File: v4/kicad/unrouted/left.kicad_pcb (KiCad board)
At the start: 2 copper layers, 160 x 118.6 mm, 68 parts

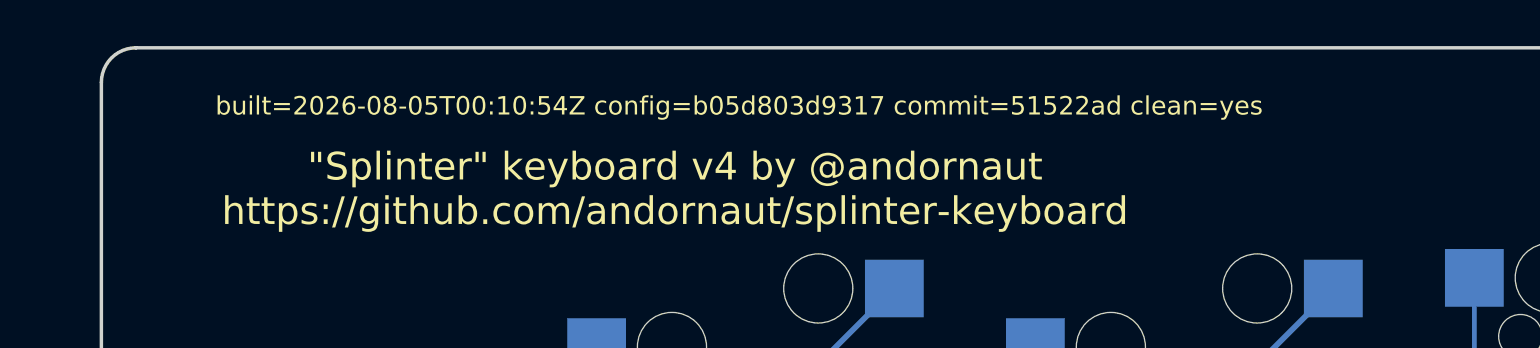
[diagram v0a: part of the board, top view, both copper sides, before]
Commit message: Rebuild the boards with the buried-copper rule in force
The right master loses the include_traces_vias stub a route had run along, plus
the collinear fragments the delete freed for the merge: 337 segments to 334. The
left half was already clean. Every gate passes.
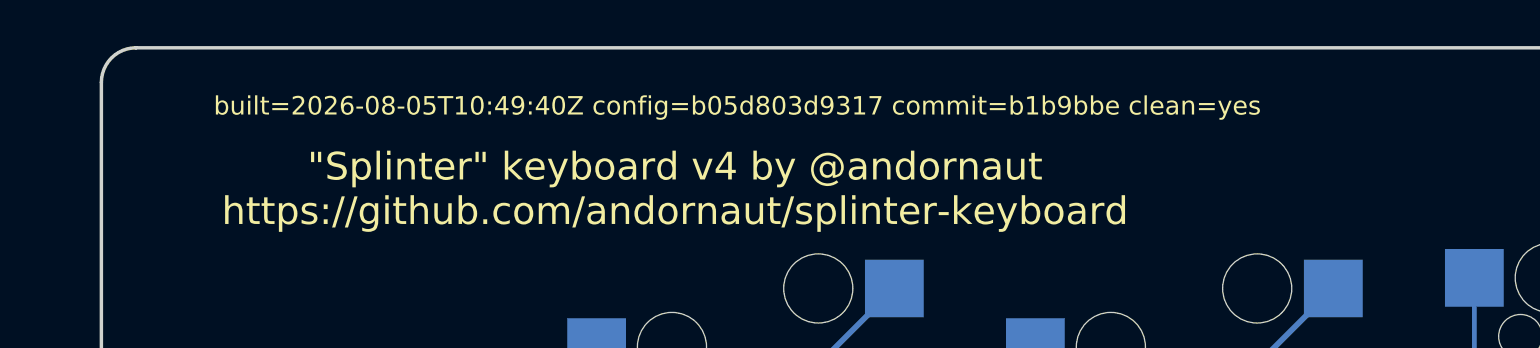
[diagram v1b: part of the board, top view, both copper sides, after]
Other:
- board text added: "built=2026-08-05T10:49:40Z config=b05d803d9317 commit=b1b9bbe clean=yes"
- board text removed: "built=2026-08-05T00:10:54Z config=b05d803d9317 commit=51522ad clean=yes"

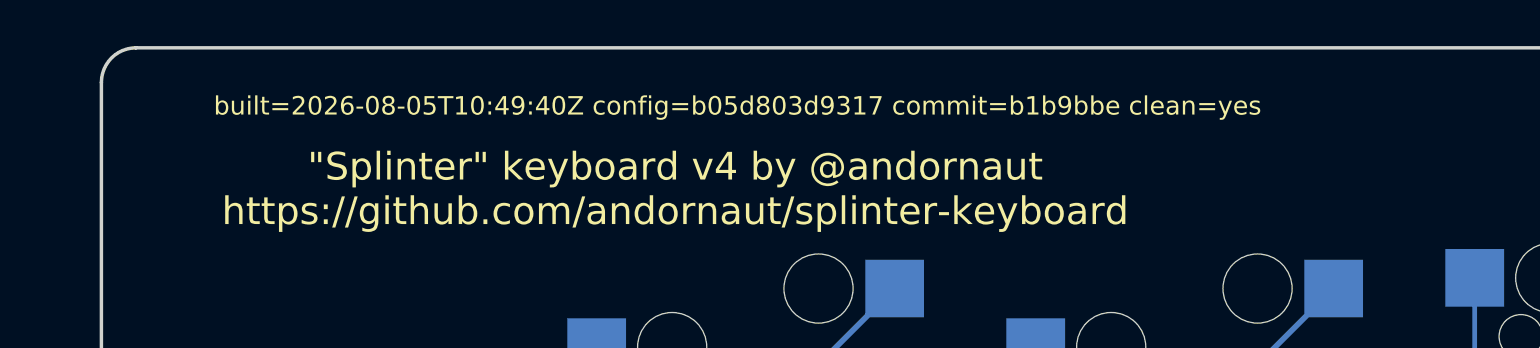
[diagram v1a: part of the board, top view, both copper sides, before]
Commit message: Rebuild the boards on the relocated scripts
Copper, pads, zones and outline are identical to the previous build; the boards
differ only in their provenance stamp and regenerated UUIDs. Every gate passes.
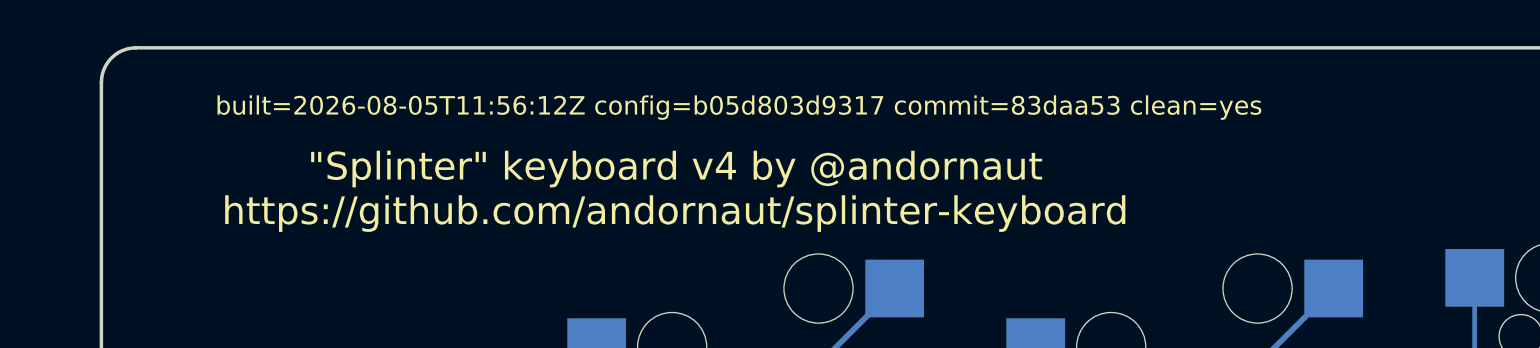
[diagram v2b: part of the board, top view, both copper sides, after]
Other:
- board text added: "built=2026-08-05T11:56:12Z config=b05d803d9317 commit=83daa53 clean=yes"
- board text removed: "built=2026-08-05T10:49:40Z config=b05d803d9317 commit=b1b9bbe clean=yes"

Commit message: Restamp the boards for the new config hash
Adding the un-filleted outlines changed the config.yaml hash, which every board's
stamp carries, so all four are restamped. Copper, pads, zones and outline are
identical to the previous build: no pcbs: entry references those outlines.
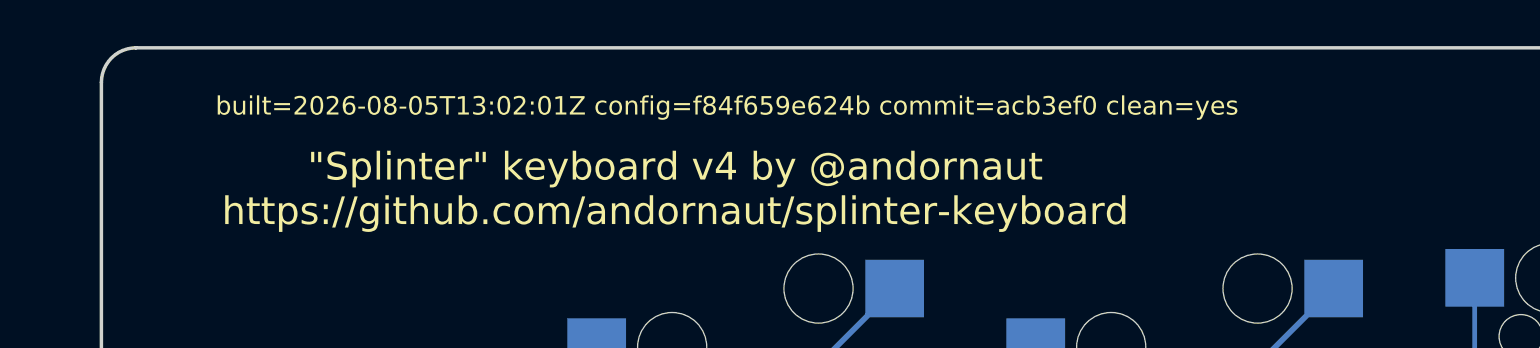
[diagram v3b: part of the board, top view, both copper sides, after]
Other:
- board text added: "built=2026-08-05T13:02:01Z config=f84f659e624b commit=acb3ef0 clean=yes"
- board text removed: "built=2026-08-05T11:56:12Z config=b05d803d9317 commit=83daa53 clean=yes"

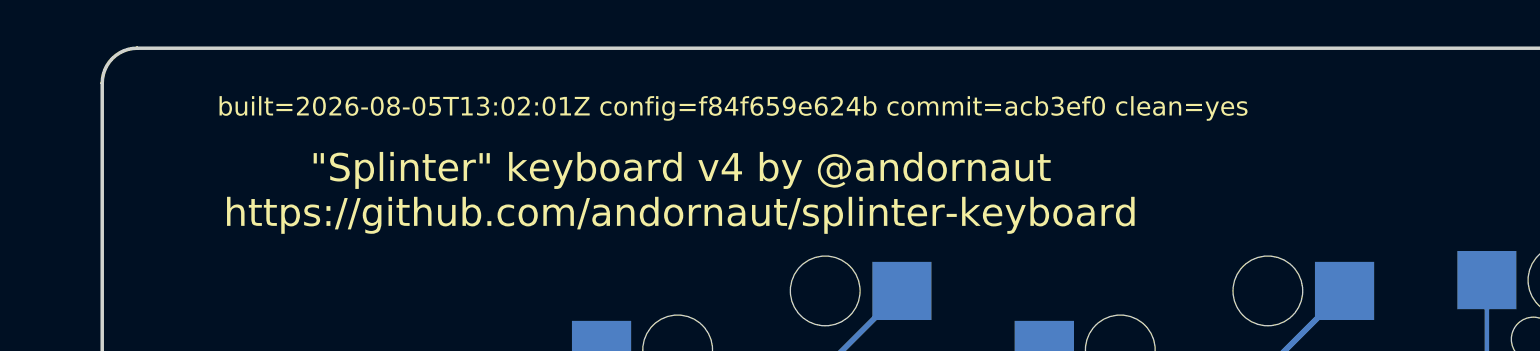
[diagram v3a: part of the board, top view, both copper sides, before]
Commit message: Restamp the boards against the reworked config comment
The stamp keys on the config hash alone, so correcting the comment above
_wallsleft_unfilleted moved every board to stale. Nothing about the design
changed: teardrops hold at 288 left and 303 right, segments at 318 and 334, and
the diff is the stamp plus regenerated UUIDs.

Built from a clean tree so commit= names the source these boards came from.
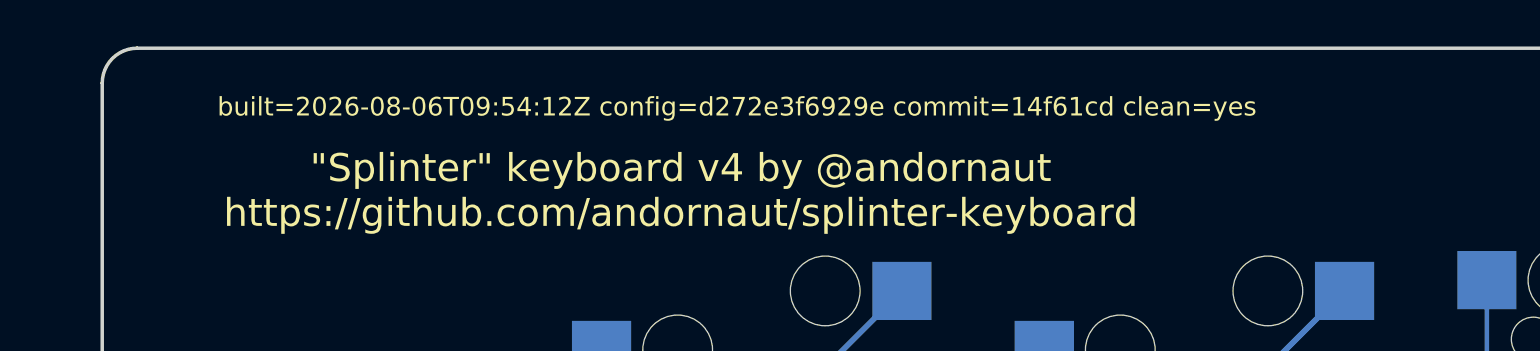
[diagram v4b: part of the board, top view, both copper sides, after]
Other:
- board text added: "built=2026-08-06T09:54:12Z config=d272e3f6929e commit=14f61cd clean=yes"
- board text removed: "built=2026-08-05T13:02:01Z config=f84f659e624b commit=acb3ef0 clean=yes"

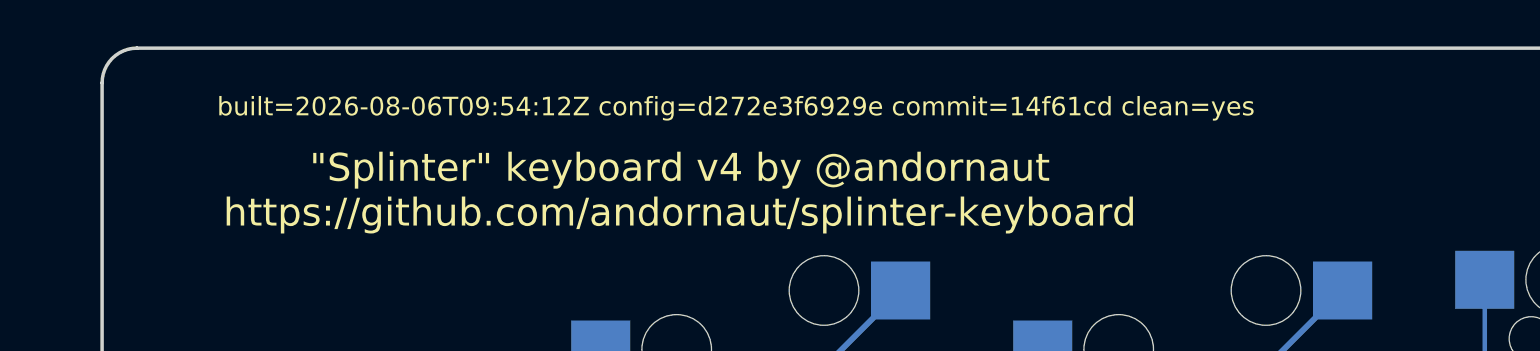
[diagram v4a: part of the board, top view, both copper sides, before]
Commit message: Rebuild the v4 boards from config d272e3f6929e
Pipeline re-run with no config change: new provenance stamp, reordered
items and re-tessellated zone fills. Tracks, vias and footprints are
unchanged on all four boards. KiCad 10 adds td_enabled and empty net
color/assignment maps to each .kicad_pro.
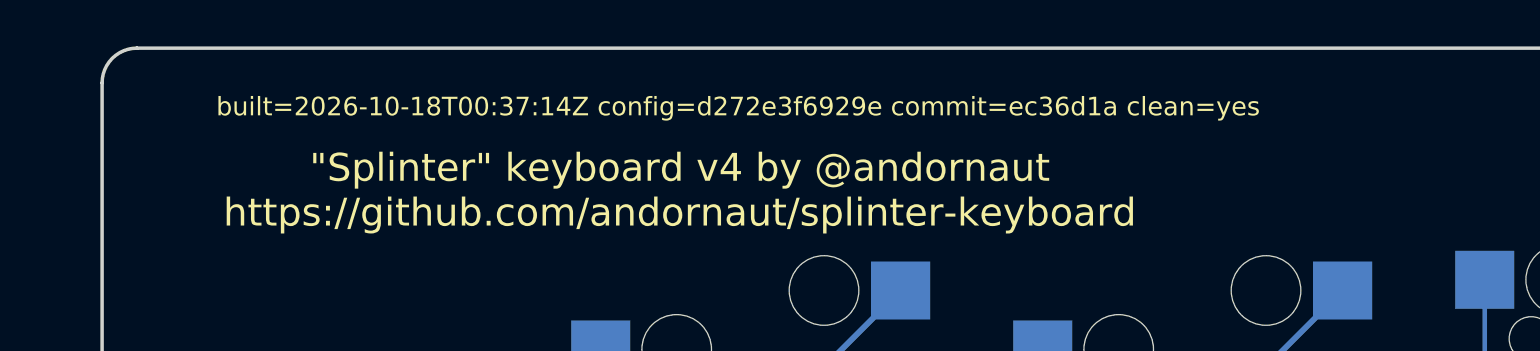
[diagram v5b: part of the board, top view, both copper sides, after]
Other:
- board text added: "built=2026-10-18T00:37:14Z config=d272e3f6929e commit=ec36d1a clean=yes"
- board text removed: "built=2026-08-06T09:54:12Z config=d272e3f6929e commit=14f61cd clean=yes"

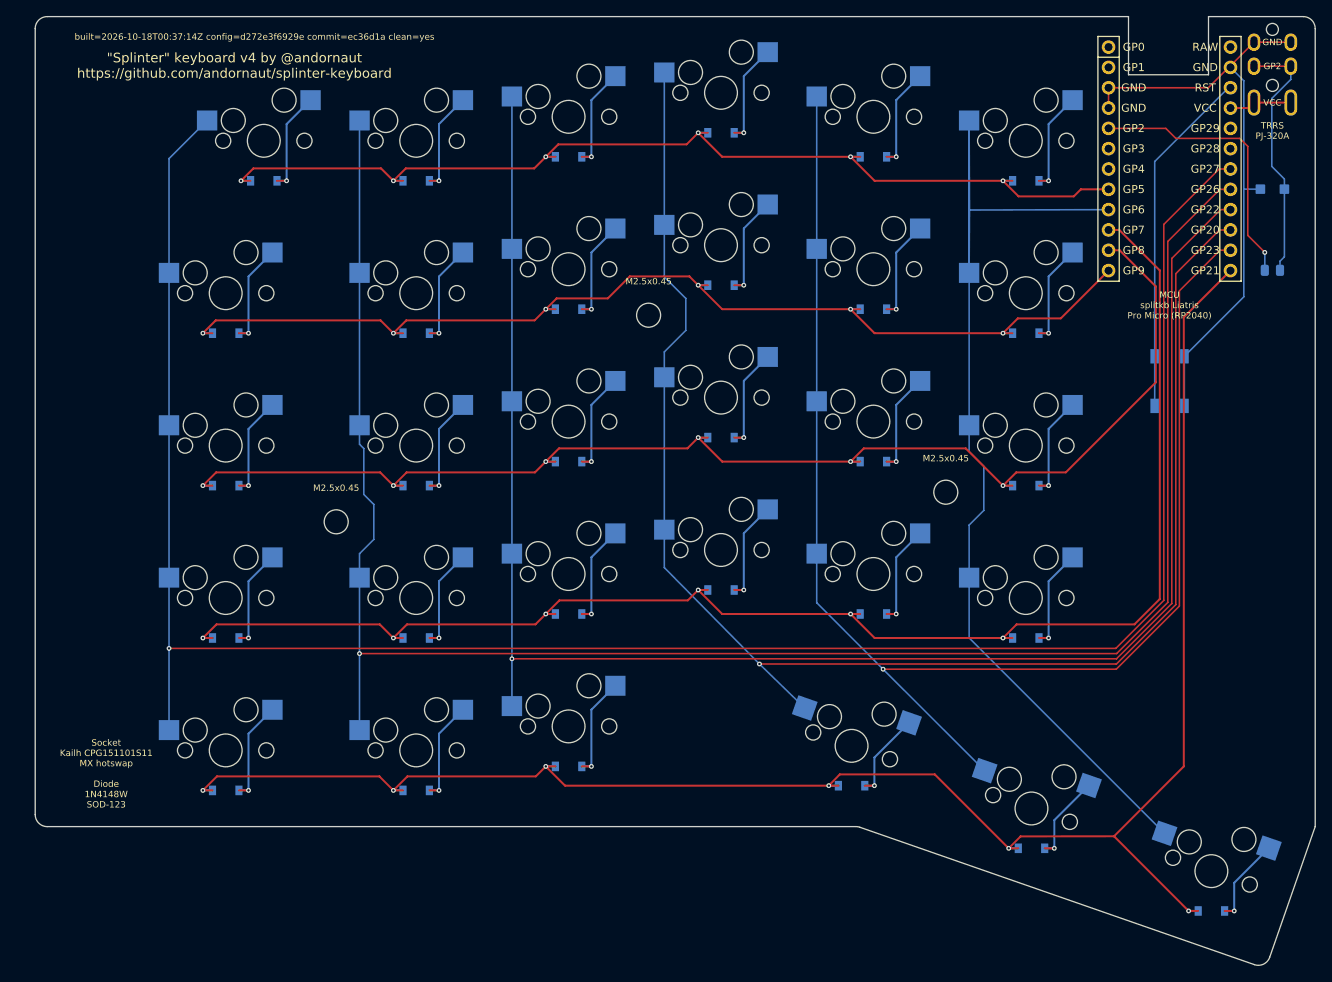
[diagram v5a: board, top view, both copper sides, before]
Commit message: Wire the v4 TRRS jack per contact and drop the data resistor
- Remove the 100R series resistor from the split data line. QMK's RP2040
  half-duplex driver has the receiving half drive the line high while the
  sender pulls it low, so series resistance lifts the low past the input
  threshold and the link fails.
- Add trrs_hc_pj320a, a single-sided HC-PJ-320A-4P-D footprint with one pad
  per contact at HCTL's recommended positions. Wire tip VCC, ring 2 GP2,
  sleeve GND and leave ring 1 open.
- Re-route the jack and TVS on both halves with the TVS in line.
- Check the jack's contact nets in validate:firmware, and treat the jack as
  non-mirrorable in validate:symmetry.
- Remove the plate wall down to the plate over the TRRS corner, with a 29.00
  relief, so no case surface can touch the jack's exposed contacts. Update
  gen-case.py, BUILD.md and the Onshape exports.
- Document the split connection, the 3.6V Liatris VCC jumper and the
  no-hot-plug rule.
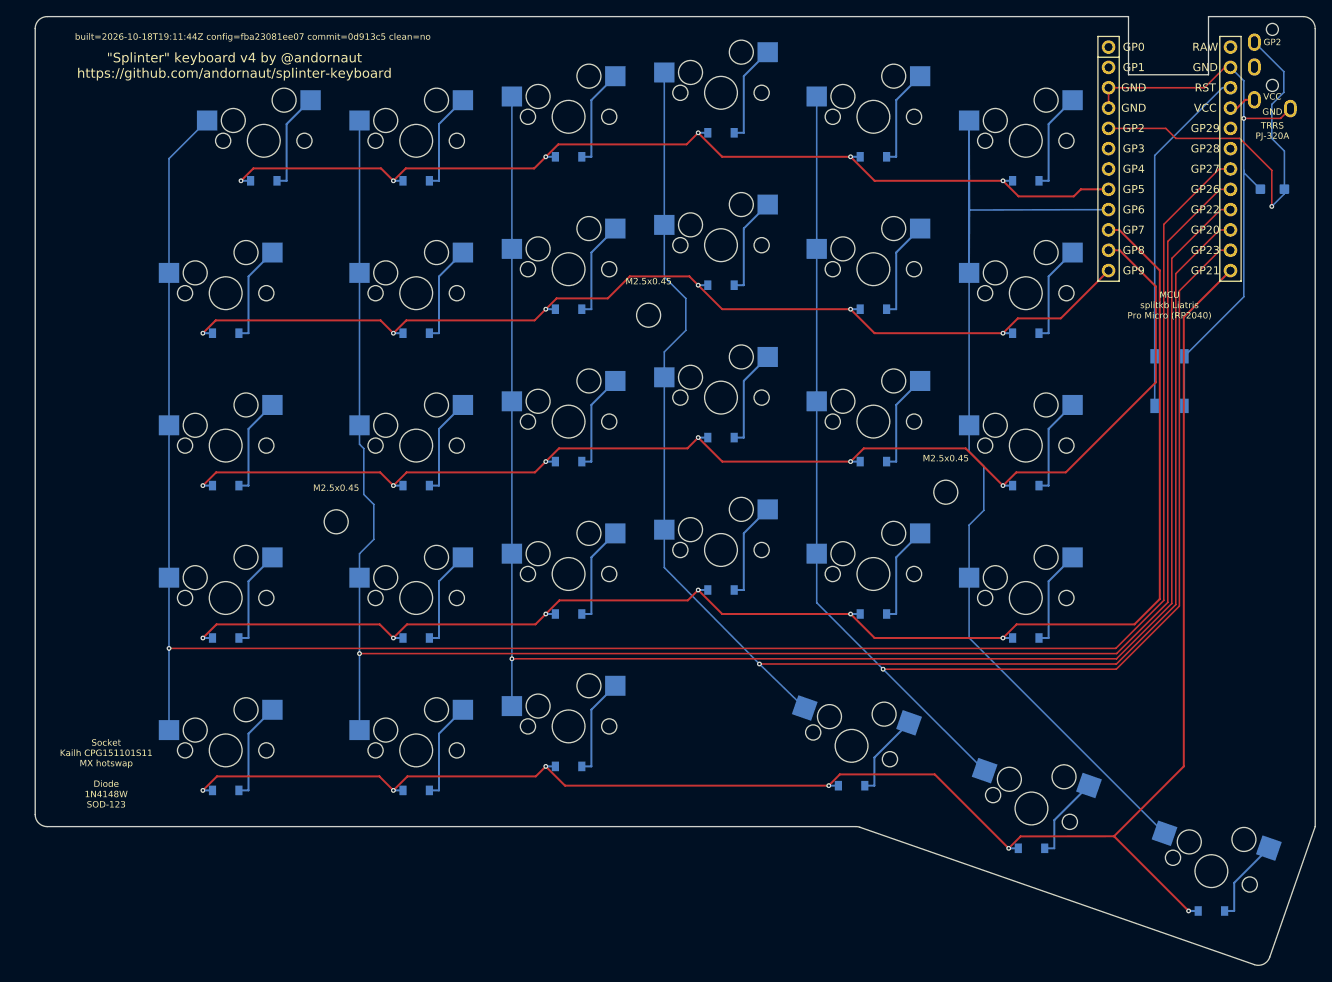
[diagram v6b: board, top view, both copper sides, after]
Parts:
- removed R1: 100R, splinter:R_0805
- TRRS1: footprint ceoloide:trrs_pj320a (reversible, symmetric) -> splinter:trrs_hc_pj320a
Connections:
- D31 pad A: DATA_RAW -> P2
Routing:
- net DATA_RAW: track 32.0 -> 0.00 mm
- net P2: track 34.7 -> 51.0 mm
- net P9: track 138.1 -> 130.9 mm
- net P8: track 166.3 -> 159.1 mm
- net P10: track 226.9 -> 219.7 mm
- net P7: track 192.0 -> 184.8 mm
- net P5: track 130.3 -> 123.1 mm
- net VCC: track 6.86 -> 2.58 mm
- net GND: track 75.2 -> 73.7 mm, vias 0 -> 1
- net five_mod: track 12.0 -> 10.8 mm, vias 1 -> 0
- net zero_upper: track 13.7 -> 12.5 mm, vias 1 -> 0
- net zero_mod: track 13.7 -> 12.5 mm, vias 1 -> 0
- net zero_lower: track 13.7 -> 12.5 mm, vias 1 -> 0
- net zero_home: track 13.7 -> 12.5 mm, vias 1 -> 0
- net three_mod: track 12.0 -> 10.8 mm, vias 1 -> 0
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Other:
- board text added: "built=2026-10-18T19:11:44Z config=fba23081ee07 commit=0d913c5 clean=no"
- board text removed: "Resistor 100R 1% UNI-ROYAL 0805W8F- 1000T5E 0805"
- board text removed: "built=2026-10-18T00:37:14Z config=d272e3f6929e commit=ec36d1a clean=yes"

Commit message: Rebuild the v4 boards from config fba23081ee07
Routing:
- net P10: track 219.7 -> 226.9 mm
- net P8: track 159.1 -> 166.3 mm
- net P9: track 130.9 -> 138.1 mm
- net P7: track 184.8 -> 192.0 mm
- net P5: track 123.1 -> 130.3 mm
- net five_mod: track 10.8 -> 12.0 mm, vias 0 -> 1
- net zero_upper: track 12.5 -> 13.7 mm, vias 0 -> 1
- net zero_mod: track 12.5 -> 13.7 mm, vias 0 -> 1
- net zero_lower: track 12.5 -> 13.7 mm, vias 0 -> 1
- net zero_home: track 12.5 -> 13.7 mm, vias 0 -> 1
- net three_mod: track 10.8 -> 12.0 mm, vias 0 -> 1
- net one_upper: track 12.5 -> 13.7 mm, vias 0 -> 1
- net one_num: track 12.5 -> 13.7 mm, vias 0 -> 1
- net one_mod: track 12.5 -> 13.7 mm, vias 0 -> 1
- net one_lower: track 12.5 -> 13.7 mm, vias 0 -> 1
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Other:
- board text added: "built=2026-10-18T19:58:37Z config=fba23081ee07 commit=c602086 clean=yes"
- board text removed: "built=2026-10-18T19:11:44Z config=fba23081ee07 commit=0d913c5 clean=no"
